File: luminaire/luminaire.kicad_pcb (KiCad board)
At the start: 2 copper layers, 18 x 89 mm, 23 parts, among them Q1 FMMT618, SW1 SW_DP3T, U1 zxsc310

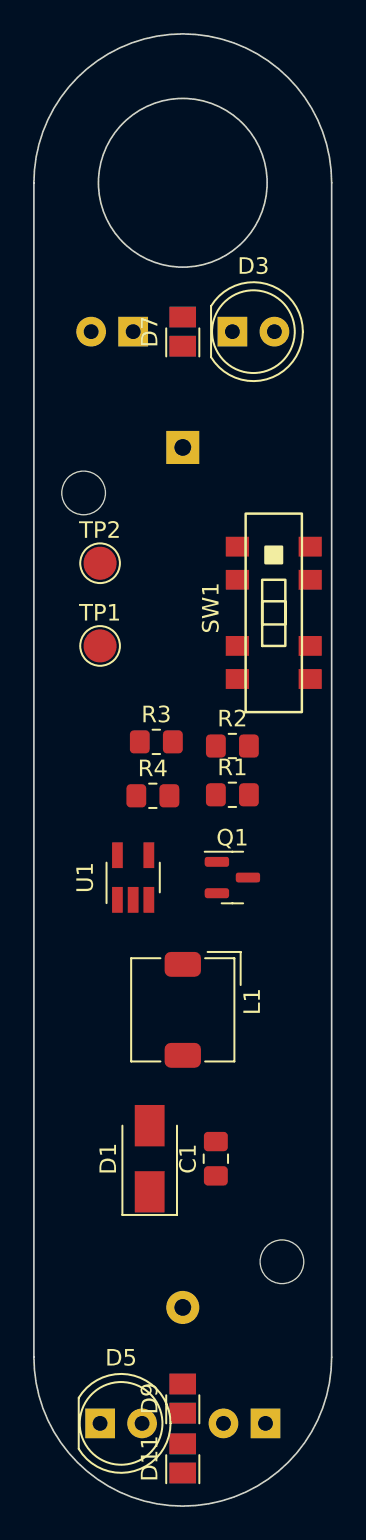
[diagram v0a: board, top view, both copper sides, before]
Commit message: Remove PTH LEDs
They are kinda massive, make layout awkward, and have really narrow
viewing angles.
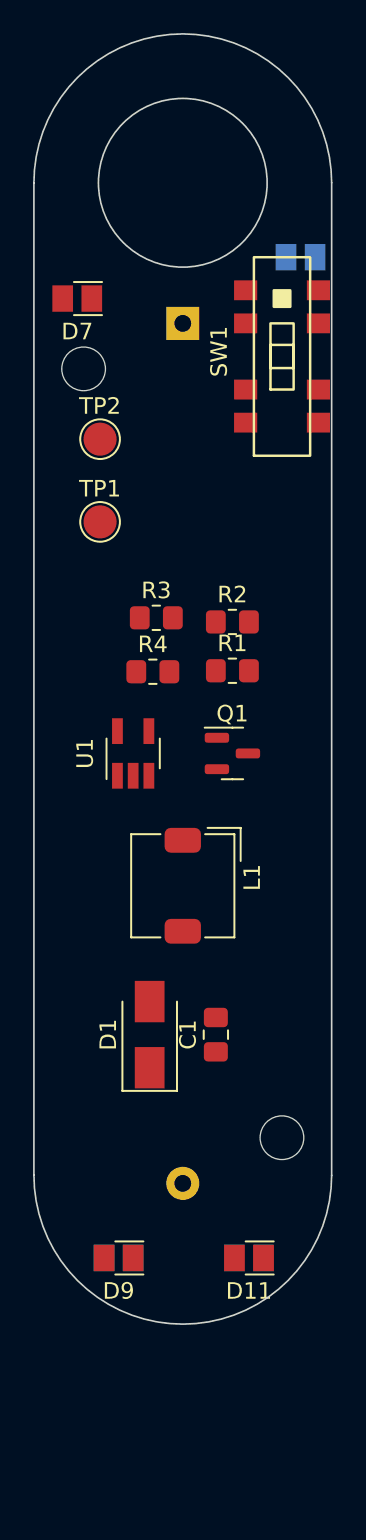
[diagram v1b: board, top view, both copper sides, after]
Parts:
- removed D2, D3, D4, D5: LED_PTH, LED_THT:LED_D5.0mm_Clear
- moved SW1 15.5 mm to (156.0, 56.5)
- moved D10 12.8 mm to (154.0, 111.0), turned to 0 degrees
- moved D11 12.8 mm to (154.0, 111.0), turned to 180 degrees
- moved D8 9.34 mm to (146.1, 111.0), turned to 0 degrees
- moved D9 9.34 mm to (146.1, 111.0), turned to 180 degrees
- moved D6 8.42 mm to (157.1, 50.5), turned to 0 degrees
- moved BT1 7.50 mm to (150.0, 54.5)
- moved C1 7.50 mm to (152.0, 97.5)
- moved D1 7.50 mm to (148.0, 97.5)
- moved L1 7.50 mm to (150.0, 88.5)
- moved Q1 7.50 mm to (153.0, 80.5)
- moved R1 7.50 mm to (153.0, 75.5)
- moved R2 7.50 mm to (153.0, 72.5)
- moved R3 7.50 mm to (148.4, 72.3)
- moved R4 7.50 mm to (148.2, 75.6)
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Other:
- board size 18 x 89 mm -> 18 x 78 mm

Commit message: Finalise design
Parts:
- moved R4 11.6 mm to (147.6, 64.0), turned to -90 degrees
- moved R3 7.68 mm to (152.8, 66.0), turned to 180 degrees
- moved R1 7.10 mm to (152.8, 68.4), turned to 180 degrees
- moved TP1 4.90 mm to (145.0, 61.6)
- moved TP2 4.30 mm to (145.0, 65.8)
- moved R2 3.66 mm to (152.8, 76.2), turned to 180 degrees
- turned L1 to 90 degrees
- turned Q1 to 180 degrees
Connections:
- D6 pad 1: Net-(D10-Pad1) -> Net-(D6-Pad1)
- D7 pad 2: Net-(D10-Pad1) -> Net-(D6-Pad1)
- U1 pad 3: Net-(BT1-Pad2) -> Net-(L1-Pad1)
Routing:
- net Net-(BT1-Pad2): track 0.00 -> 81.0 mm, vias 0 -> 2
- net Net-(C1-Pad1): track 0.00 -> 80.4 mm, vias 0 -> 1
- net Net-(D11-Pad1): track 0.00 -> 71.2 mm, vias 0 -> 2
- net Net-(L1-Pad1): track 0.00 -> 56.4 mm, vias 0 -> 2
- net Net-(D9-Pad1): track 0.00 -> 50.1 mm
- net Net-(SW1-Pad7): track 0.00 -> 28.3 mm, vias 0 -> 2
- net Net-(Q1-Pad2): track 0.00 -> 26.7 mm, vias 0 -> 2
- net Net-(D1-Pad2): track 0.00 -> 20.2 mm, vias 0 -> 2
- net Net-(R1-Pad2): track 0.00 -> 19.7 mm
- net Net-(Q1-Pad1): track 0.00 -> 18.3 mm
- net Net-(D6-Pad1): track 0.00 -> 15.3 mm, vias 0 -> 1
- net Net-(BT1-Pad1): track 0.00 -> 12.5 mm
- net Net-(D8-Pad1): track 0.00 -> 4.18 mm, vias 0 -> 1
- net Net-(D10-Pad1): track 0.00 -> 3.04 mm, vias 0 -> 1
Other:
- board text added: "DAVID TURNER - JUNE 2022"
- board text added: "LUMINAIRE"

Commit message: Finalise BOM and gerbers
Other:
- board text added: "JLCJLCJLCJLC"
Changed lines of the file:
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@@
   (setup
     (stackup
-      (layer "F.SilkS" (type "Top Silk Screen"))
+      (layer "F.SilkS" (type "Top Silk Screen") (color "Black"))
       (layer "F.Paste" (type "Top Solder Paste"))
-      (layer "F.Mask" (type "Top Solder Mask") (thickness 0.01))
+      (layer "F.Mask" (type "Top Solder Mask") (color "White") (thickness 0.01))
       (layer "F.Cu" (type "copper") (thickness 0.035))
       (layer "dielectric 1" (type "core") (thickness 1.51) (material "FR4") (epsilon_r 4.5) (loss_tangent 0.02))
       (layer "B.Cu" (type "copper") (thickness 0.035))
-      (layer "B.Mask" (type "Bottom Solder Mask") (thickness 0.01))
+      (layer "B.Mask" (type "Bottom Solder Mask") (color "White") (thickness 0.01))
       (layer "B.Paste" (type "Bottom Solder Paste"))
-      (layer "B.SilkS" (type "Bottom Silk Screen"))
+      (layer "B.SilkS" (type "Bottom Silk Screen") (color "Black"))
       (copper_finish "None")
       (dielectric_constraints no)
@@
     (pad_to_mask_clearance 0)
     (pcbplotparams
-      (layerselection 0x00010fc_ffffffff)
+      (layerselection 0x00010f8_ffffffff)
       (disableapertmacros false)
-      (usegerberextensions false)
+      (usegerberextensions true)
       (usegerberattributes true)
       (usegerberadvancedattributes true)
@@
       (outputformat 1)
       (mirror false)
-      (drillshape 1)
+      (drillshape 0)
       (scaleselection 1)
-      (outputdirectory "")
+      (outputdirectory "gerbers")
     )
   )
@@
     (fp_line (start -1 0.625) (end -1 -0.625) (layer "F.Fab") (width 0.1))
     (fp_line (start 1 -0.625) (end 1 0.625) (layer "F.Fab") (width 0.1))
-    (pad "1" smd roundrect (at -1 0 180) (size 1.2 1.4) (layers "F.Cu" "F.Paste" "F.Mask") (roundrect_rratio 0.208333)
+    (pad "1" smd roundrect (at -1 0 180) (size 1.2 1.4) (layers "F.Cu" "F.Paste" "F.Mask") (roundrect_rratio 0.2083333333)
       (net 6 "Net-(Q1-Pad2)") (pintype "passive"))
-    (pad "2" smd roundrect (at 1 0 180) (size 1.2 1.4) (layers "F.Cu" "F.Paste" "F.Mask") (roundrect_rratio 0.208333)
+    (pad "2" smd roundrect (at 1 0 180) (size 1.2 1.4) (layers "F.Cu" "F.Paste" "F.Mask") (roundrect_rratio 0.2083333333)
       (net 7 "Net-(R1-Pad2)") (pintype "passive"))
     (model "${KICAD6_3DMODEL_DIR}/Resistor_SMD.3dshapes/R_0805_2012Metric.wrl"
@@
   (footprint "CL-SB-23B-0XX:CL-SB-23B-0XX" (layer "F.Cu")
     (at 156 56.5 90)
+    (property "Farnell" "2978768")
     (property "Sheetfile" "luminaire.kicad_sch")
     (property "Sheetname" "")
@@
     (fp_line (start 1 0.625) (end -1 0.625) (layer "F.Fab") (width 0.1))
     (fp_line (start 1 -0.625) (end 1 0.625) (layer "F.Fab") (width 0.1))
-    (pad "1" smd roundrect (at -1.0375 0 90) (size 1.175 1.45) (layers "F.Cu" "F.Paste" "F.Mask") (roundrect_rratio 0.212766)
+    (pad "1" smd roundrect (at -1.0375 0 90) (size 1.175 1.45) (layers "F.Cu" "F.Paste" "F.Mask") (roundrect_rratio 0.2127659574)
       (net 11 "Net-(C1-Pad1)") (pintype "passive"))
-    (pad "2" smd roundrect (at 1.0375 0 90) (size 1.175 1.45) (layers "F.Cu" "F.Paste" "F.Mask") (roundrect_rratio 0.212766)
+    (pad "2" smd roundrect (at 1.0375 0 90) (size 1.175 1.45) (layers "F.Cu" "F.Paste" "F.Mask") (roundrect_rratio 0.2127659574)
       (net 2 "Net-(BT1-Pad2)") (pintype "passive"))
     (model "${KICAD6_3DMODEL_DIR}/Capacitor_SMD.3dshapes/C_0805_2012Metric.wrl"
@@
     (fp_line (start 1 0.625) (end -1 0.625) (layer "F.Fab") (width 0.1))
     (fp_line (start -1 0.625) (end -1 -0.625) (layer "F.Fab") (width 0.1))
-    (pad "1" smd roundrect (at -1 0 180) (size 1.2 1.4) (layers "F.Cu" "F.Paste" "F.Mask") (roundrect_rratio 0.208333)
+    (pad "1" smd roundrect (at -1 0 180) (size 1.2 1.4) (layers "F.Cu" "F.Paste" "F.Mask") (roundrect_rratio 0.2083333333)
       (net 6 "Net-(Q1-Pad2)") (pintype "passive"))
-    (pad "2" smd roundrect (at 1 0 180) (size 1.2 1.4) (layers "F.Cu" "F.Paste" "F.Mask") (roundrect_rratio 0.208333)
+    (pad "2" smd roundrect (at 1 0 180) (size 1.2 1.4) (layers "F.Cu" "F.Paste" "F.Mask") (roundrect_rratio 0.2083333333)
       (net 2 "Net-(BT1-Pad2)") (pintype "passive"))
     (model "${KICAD6_3DMODEL_DIR}/Resistor_SMD.3dshapes/R_0805_2012Metric.wrl"
@@
     (fp_line (start -1 0.625) (end -1 -0.625) (layer "F.Fab") (width 0.1))
     (fp_line (start -1 -0.625) (end 1 -0.625) (layer "F.Fab") (width 0.1))
-    (pad "1" smd roundrect (at -1 0 180) (size 1.2 1.4) (layers "F.Cu" "F.Paste" "F.Mask") (roundrect_rratio 0.208333)
+    (pad "1" smd roundrect (at -1 0 180) (size 1.2 1.4) (layers "F.Cu" "F.Paste" "F.Mask") (roundrect_rratio 0.2083333333)
       (net 7 "Net-(R1-Pad2)") (pintype "passive"))
-    (pad "2" smd roundrect (at 1 0 180) (size 1.2 1.4) (layers "F.Cu" "F.Paste" "F.Mask") (roundrect_rratio 0.208333)
+    (pad "2" smd roundrect (at 1 0 180) (size 1.2 1.4) (layers "F.Cu" "F.Paste" "F.Mask") (roundrect_rratio 0.2083333333)
       (net 2 "Net-(BT1-Pad2)") (pintype "passive"))
     (model "${KICAD6_3DMODEL_DIR}/Resistor_SMD.3dshapes/R_0805_2012Metric.wrl"
@@
     (fp_line (start -1 0.625) (end -1 -0.625) (layer "F.Fab") (width 0.1))
     (fp_line (start 1 0.625) (end -1 0.625) (layer "F.Fab") (width 0.1))
-    (pad "1" smd roundrect (at -1 0 270) (size 1.2 1.4) (layers "F.Cu" "F.Paste" "F.Mask") (roundrect_rratio 0.208333)
+    (pad "1" smd roundrect (at -1 0 270) (size 1.2 1.4) (layers "F.Cu" "F.Paste" "F.Mask") (roundrect_rratio 0.2083333333)
       (net 2 "Net-(BT1-Pad2)") (pintype "passive"))
-    (pad "2" smd roundrect (at 1 0 270) (size 1.2 1.4) (layers "F.Cu" "F.Paste" "F.Mask") (roundrect_rratio 0.208333)
+    (pad "2" smd roundrect (at 1 0 270) (size 1.2 1.4) (layers "F.Cu" "F.Paste" "F.Mask") (roundrect_rratio 0.2083333333)
       (net 16 "Net-(D9-Pad1)") (pintype "passive"))
     (model "${KICAD6_3DMODEL_DIR}/Resistor_SMD.3dshapes/R_0805_2012Metric.wrl"
@@
   (gr_line (start 159 106) (end 159 46) (layer "Edge.Cuts") (width 0.1))
   (gr_line (start 141 46) (end 141 106) (layer "Edge.Cuts") (width 0.1))
+  (gr_text "JLCJLCJLCJLC" (at 143.8 99.2 90) (layer "B.SilkS")
+    (effects (font (size 1.5 1.5) (thickness 0.2)) (justify mirror))
+  )
   (gr_text "DAVID TURNER - JUNE 2022" (at 143.2 86.6 90) (layer "F.SilkS")
     (effects (font (size 1.5 1.5) (thickness 0.2)))
